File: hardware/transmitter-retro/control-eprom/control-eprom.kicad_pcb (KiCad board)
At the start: 2 copper layers, 100 x 90 mm, 15 parts, among them J4 Expansion, U18 74LS32, U20 74LS00, U3 74LS161, U4 74LS161, U5 27128

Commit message: Update part numbers Swap out input connector footprint Placement tweaks
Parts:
- removed C18, C20: .01uF, Capacitor_THT:C_Rect_L4.6mm_W2.0mm_P2.50mm_MKS02_FKP02
- removed J4: Expansion, Connector_PinHeader_2.54mm:PinHeader_2x20_P2.54mm_Vertical
- removed U18: 74LS32, Package_DIP:DIP-14_W7.62mm
- removed U20: 74LS00, Package_DIP:DIP-14_W7.62mm
- added C1: .01uF, Capacitor_THT:C_Rect_L4.6mm_W2.0mm_P2.50mm_MKS02_FKP02, F.Cu at (175.3, 70.1)
- added C2: .01uF, Capacitor_THT:C_Rect_L4.6mm_W2.0mm_P2.50mm_MKS02_FKP02, F.Cu at (180.5, 70.1)
- added J1: Expansion, Connector_PinHeader_2.54mm:PinHeader_2x20_P2.54mm_Vertical, F.Cu at (149.9, 70.7)
- added U1: 74LS32, Package_DIP:DIP-14_W7.62mm, F.Cu at (155.4, 70.4)
- added U2: 74LS00, Package_DIP:DIP-14_W7.62mm, F.Cu at (165.3, 70.4)
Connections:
- U5 pad 17: /SHIFT_DISABLE -> /~SHIFT_ENABLE

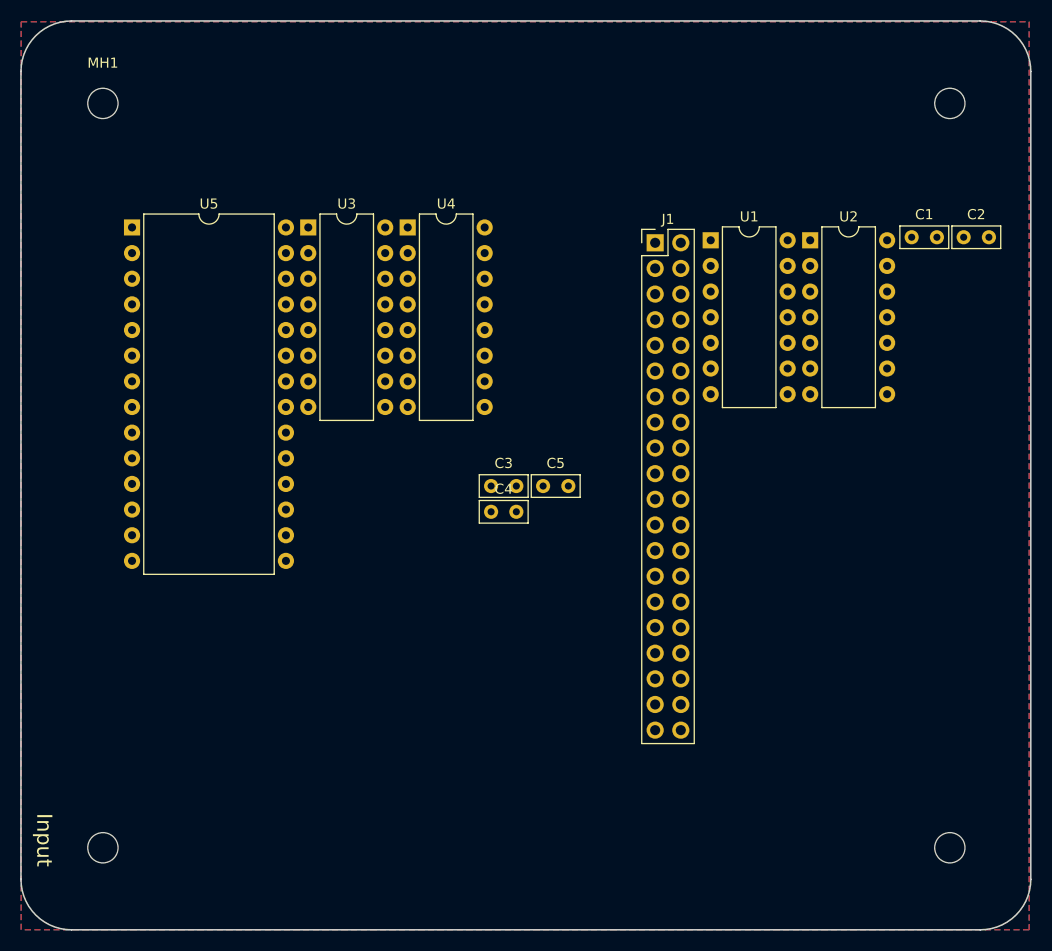
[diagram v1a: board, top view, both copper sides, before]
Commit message: Prototype and PCB layout for core Prototype and PCB layout for demo Prototype and PCB layout for control-eprom Move display design forward Refactor control-dmx to dmx Update expansion connector on all boards Add test suites Add tx-retro readme Cleanup
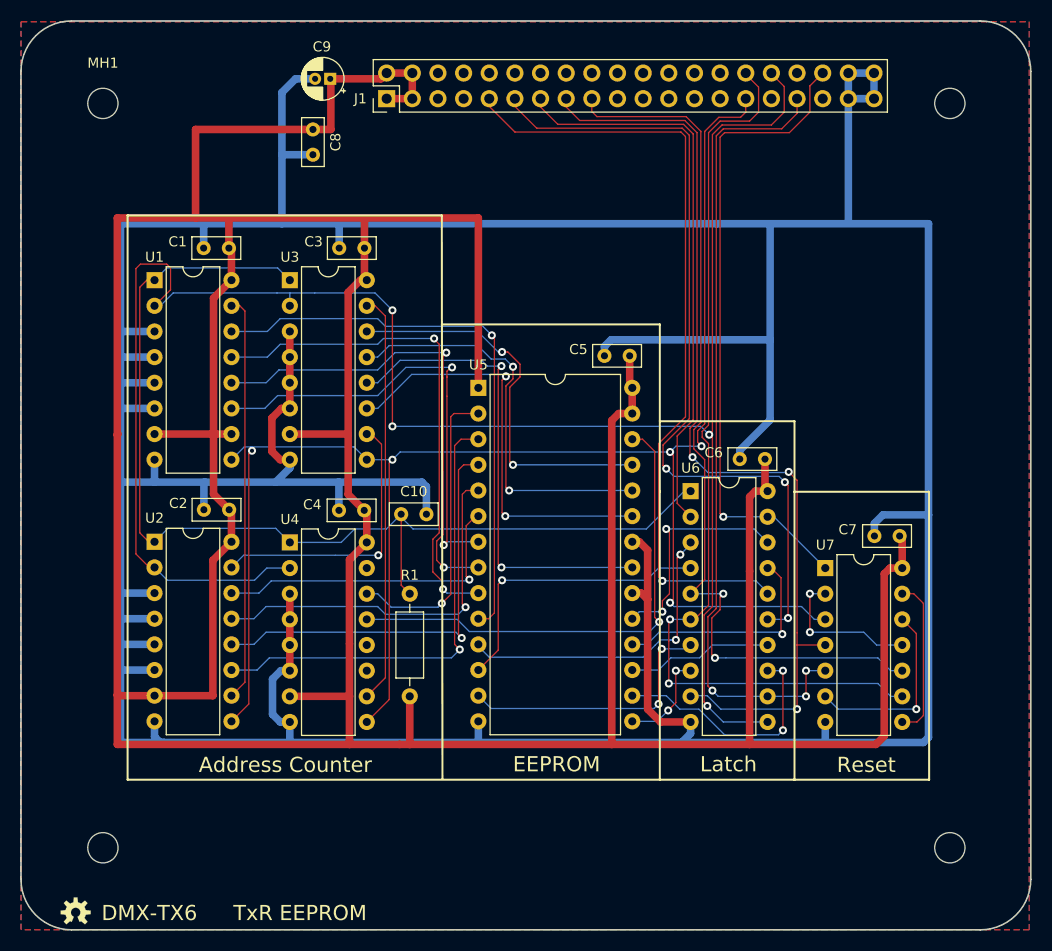
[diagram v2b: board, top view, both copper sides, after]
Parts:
- added ?: , footprints:OSHW-LOGO-S, F.Cu at (92.5, 137.0)
- added C10: 0.1uF, Capacitor_THT:C_Rect_L4.6mm_W2.0mm_P2.50mm_MKS02_FKP02, F.Cu at (124.8, 97.5)
- added C6: 0.1uF, Capacitor_THT:C_Rect_L4.6mm_W2.0mm_P2.50mm_MKS02_FKP02, F.Cu at (160.8, 92.1)
- added C7: 0.1uF, Capacitor_THT:C_Rect_L4.6mm_W2.0mm_P2.50mm_MKS02_FKP02, F.Cu at (174.1, 99.7)
- added C8: 0.1uF, Capacitor_THT:C_Rect_L4.6mm_W2.0mm_P2.50mm_MKS02_FKP02, F.Cu at (116.0, 59.4)
- added C9: 10uF, Capacitor_THT:CP_Radial_D4.0mm_P1.50mm, F.Cu at (117.7, 54.4)
- added G***: LOGO, footprints:logo_cr_5x5, B.Cu at (105.7, 131.6)
- added R1: 10k, Resistor_THT:R_Axial_DIN0207_L6.3mm_D2.5mm_P10.16mm_Horizontal, F.Cu at (125.6, 115.6)
- added U6: 74LS273, Package_DIP:DIP-20_W7.62mm, F.Cu at (153.4, 95.2)
- added U7: 74LS32, Package_DIP:DIP-14_W7.62mm, F.Cu at (166.8, 102.9)
- C1, C2, C3, C4, C5: value .01uF -> 0.1uF
- U1: value 74LS32 -> 74LS161; footprint Package_DIP:DIP-14_W7.62mm -> Package_DIP:DIP-16_W7.62mm
- U2: value 74LS00 -> 74LS161; footprint Package_DIP:DIP-14_W7.62mm -> Package_DIP:DIP-16_W7.62mm
- moved C2 77.6 mm to (107.7, 97.1), turned to 180 degrees
- moved U2 71.5 mm to (100.3, 100.3)
- moved C1 67.6 mm to (107.7, 71.2), turned to 180 degrees
- moved U1 55.2 mm to (100.3, 74.4)
- moved U5 37.8 mm to (132.4, 85.0)
- moved U4 33.3 mm to (113.7, 100.3)
- moved J1 30.2 mm to (123.3, 56.4), turned to 90 degrees
- moved C3 26.7 mm to (121.1, 71.2), turned to 180 degrees
- moved C5 15.5 mm to (147.4, 81.9), turned to 180 degrees
- moved C4 12.6 mm to (121.1, 97.2), turned to 180 degrees
- moved U3 5.53 mm to (113.7, 74.4)
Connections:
- net Net-(U3-Pad15) renamed /CARRY_2
- J1 pad 10: /SAMPLE_LATCH -> Net-(J1-Pad10)
- J1 pad 11: Net-(J1-Pad11) -> /SAMPLE_SEL0
- J1 pad 12: /~SAMPLE_RESET -> Net-(J1-Pad12)
- J1 pad 13: Net-(J1-Pad13) -> /DATA_FIXED
- J1 pad 14: /SAMPLE_SEL0 -> Net-(J1-Pad14)
- J1 pad 15: Net-(J1-Pad15) -> /~SHIFT_LOAD
- J1 pad 16: /SAMPLE_SEL1 -> Net-(J1-Pad16)
- J1 pad 17: Net-(J1-Pad17) -> /SHIFT_TRANSMIT
- J1 pad 18: /~SHIFT_LOAD -> Net-(J1-Pad18)
- J1 pad 20: /~SHIFT_ENABLE -> Net-(J1-Pad20)
- J1 pad 22: /SHIFT_TRANSMIT -> Net-(J1-Pad22)
- J1 pad 26: /~FRAME_RESET -> Net-(J1-Pad26)
- J1 pad 29: /CLK_TX -> /~FRAME_RESET
- J1 pad 30: /DATA_FIXED -> /~SHIFT_ENABLE
- J1 pad 32: Net-(J1-Pad32) -> /CLK_TX
- J1 pad 33: GND -> /~SAMPLE_RESET
- J1 pad 35: GND -> Net-(J1-Pad35)
- J1 pad 36: Net-(J1-Pad36) -> /SAMPLE_LATCH
- J1 pad 38: Net-(J1-Pad38) -> GND
- J1 pad 40: Net-(J1-Pad40) -> GND
- J1 pad 9: Net-(J1-Pad9) -> /SAMPLE_SEL1
- U1 pad 1: /SHIFT_TRANSMIT -> Net-(C10-Pad1)
- U1 pad 10: Net-(U1-Pad10) -> +5V
- U1 pad 11: /~FRAME_RESET -> /IA3
- U1 pad 12: Net-(U1-Pad12) -> /IA2
- U1 pad 13: Net-(U1-Pad13) -> /IA1
- U1 pad 14: +5V -> /IA0
- U1 pad 2: /~SHIFT_ENABLE -> /CLK_TX
- U1 pad 3: Net-(U1-Pad10) -> GND
- U1 pad 4: /~SAMPLE_RESET -> GND
- U1 pad 5: /~SHIFT_LOAD -> GND
- U1 pad 6: Net-(U1-Pad13) -> GND
- U1 pad 7: GND -> +5V
- U1 pad 8: Net-(U1-Pad12) -> GND
- U1 pad 9: Net-(U1-Pad9) -> /~FRAME_RESET
- U2 pad 1: /DATA_FIXED -> Net-(C10-Pad1)
- U2 pad 10: +5V -> /CARRY_0
- U2 pad 11: Net-(U2-Pad11) -> /IA7
- U2 pad 12: +5V -> /IA6
- U2 pad 13: +5V -> /IA5
- U2 pad 14: +5V -> /IA4
- U2 pad 2: /SAMPLE_LATCH -> /CLK_TX
- U2 pad 3: Net-(U1-Pad9) -> GND
- U2 pad 4: +5V -> GND
- U2 pad 5: +5V -> GND
- U2 pad 6: Net-(U2-Pad6) -> GND
- U2 pad 7: GND -> +5V
- U2 pad 8: Net-(U2-Pad8) -> GND
- U2 pad 9: +5V -> /~FRAME_RESET
- U3 pad 1: /~FRAME_RESET -> Net-(C10-Pad1)
- U3 pad 10: +5V -> /CARRY_1
- U3 pad 11: /IA3 -> /IA11
- U3 pad 12: /IA2 -> /IA10
- U3 pad 13: /IA1 -> /IA9
- U3 pad 14: /IA0 -> /IA8
- U3 pad 9: +5V -> /~FRAME_RESET
- U4 pad 1: /~FRAME_RESET -> Net-(C10-Pad1)
- U4 pad 11: /IA7 -> Net-(U4-Pad11)
- U4 pad 12: /IA6 -> Net-(U4-Pad12)
- U4 pad 13: /IA5 -> /IA13
- U4 pad 14: /IA4 -> /IA12
- U4 pad 9: +5V -> /~FRAME_RESET
- U5 pad 11: /SAMPLE_LATCH -> Net-(U5-Pad11)
- U5 pad 12: /~SAMPLE_RESET -> Net-(U5-Pad12)
- U5 pad 13: /SAMPLE_SEL0 -> Net-(U5-Pad13)
- U5 pad 15: /SAMPLE_SEL1 -> Net-(U5-Pad15)
- U5 pad 16: /~SHIFT_LOAD -> Net-(U5-Pad16)
- U5 pad 17: /~SHIFT_ENABLE -> Net-(U5-Pad17)
- U5 pad 18: /SHIFT_TRANSMIT -> Net-(U5-Pad18)
- U5 pad 19: /DATA_FIXED -> Net-(U5-Pad19)
- U5 pad 2: GND -> /IA12
- U5 pad 21: GND -> /IA10
- U5 pad 23: GND -> /IA11
- U5 pad 24: GND -> /IA9
- U5 pad 25: GND -> /IA8
- U5 pad 26: GND -> /IA13
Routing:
- net GND: track 0.00 -> 495.4 mm
- net +5V: track 0.00 -> 451.1 mm
- net /CLK_TX: track 0.00 -> 199.6 mm, vias 0 -> 4
- net /~FRAME_RESET: track 0.00 -> 172.6 mm, vias 0 -> 5
- net Net-(C10-Pad1): track 0.00 -> 108.2 mm
- net /~SHIFT_LOAD: track 0.00 -> 95.3 mm, vias 0 -> 3
- net /~SHIFT_ENABLE: track 0.00 -> 92.1 mm, vias 0 -> 2
- net /SHIFT_TRANSMIT: track 0.00 -> 89.2 mm, vias 0 -> 2
- net /SAMPLE_SEL0: track 0.00 -> 81.4 mm, vias 0 -> 3
- net /~SAMPLE_RESET: track 0.00 -> 80.1 mm, vias 0 -> 3
- net /SAMPLE_SEL1: track 0.00 -> 77.7 mm, vias 0 -> 1
- net /SAMPLE_LATCH: track 0.00 -> 64.2 mm, vias 0 -> 1
- net /IA0: track 0.00 -> 56.4 mm, vias 0 -> 1
- net /DATA_FIXED: track 0.00 -> 56.2 mm
- net /IA1: track 0.00 -> 50.2 mm, vias 0 -> 2
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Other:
- net class Default: trace_width 0.25 -> 0.127
- net class Gnd added: clearance 0.25, trace_width 0.75, via_dia 0.8, via_drill 0.4
- net class Power added: clearance 0.25, trace_width 0.75, via_dia 0.8, via_drill 0.4
- rule trace_min: 0.2 -> 0.127
- rule via_min_size: 0.4 -> 0.5
- board text added: "Address Counter"
- board text added: "DMX-TX6"
- board text added: "DMX-TX6, Rev 1.0 Crazy Giraffe Software"
- board text added: "EEPROM"
- board text added: "Latch"
- board text added: "Reset"
- board text added: "TxR EEPROM"
- board text removed: "DMX-TX5, Rev 1.2 Crazy Giraffe Software"
- board text removed: "Input"

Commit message: Rev 1.1 - Value labels - 74LS06 led driver
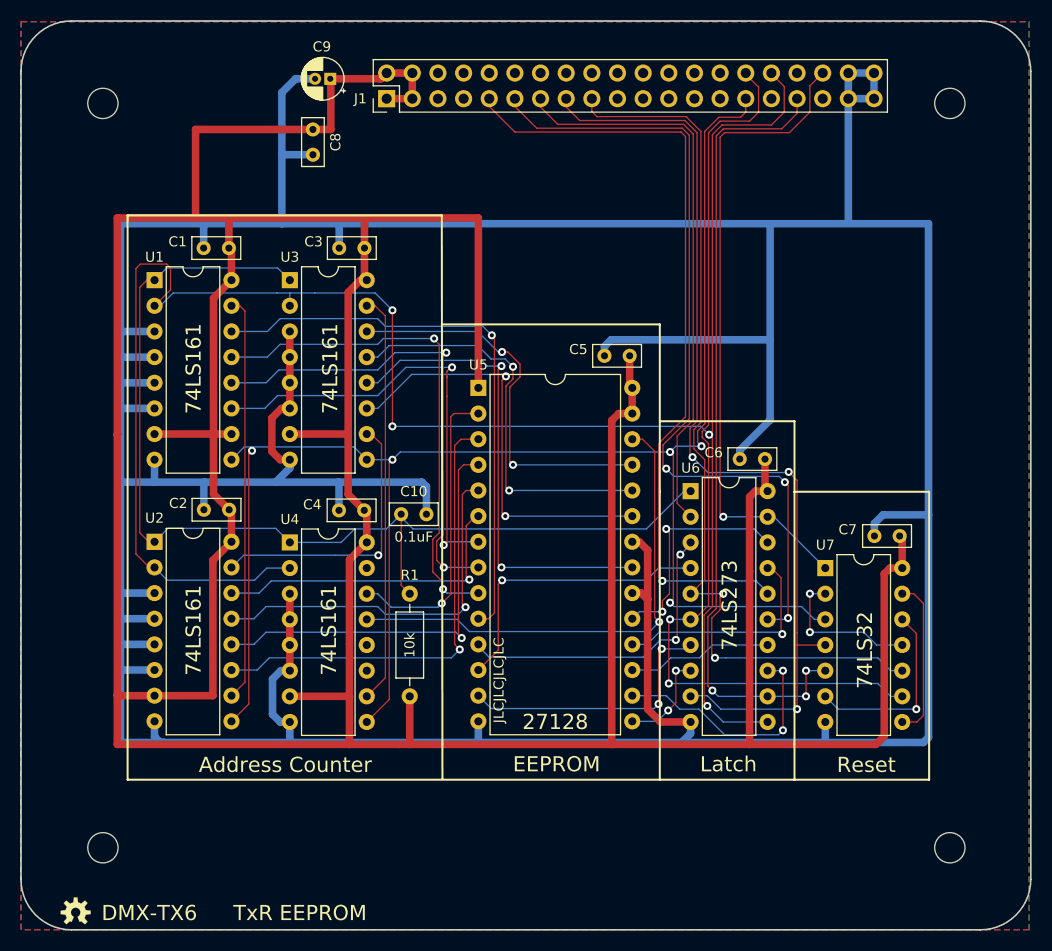
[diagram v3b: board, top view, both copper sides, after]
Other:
- board text added: "27128"
- board text added: "74LS161"
- board text added: "74LS273"
- board text added: "74LS32"
- board text added: "DMX-TX6, Rev 1.1 Crazy Giraffe Software"
- board text added: "JLCJLCJLCJLC"
- board text removed: "DMX-TX6, Rev 1.0 Crazy Giraffe Software"
